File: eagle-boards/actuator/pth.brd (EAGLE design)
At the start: 59.4 x 53.3 mm, 9 parts, among them IC1 ULN2003AN, IC2 ULN2003AN

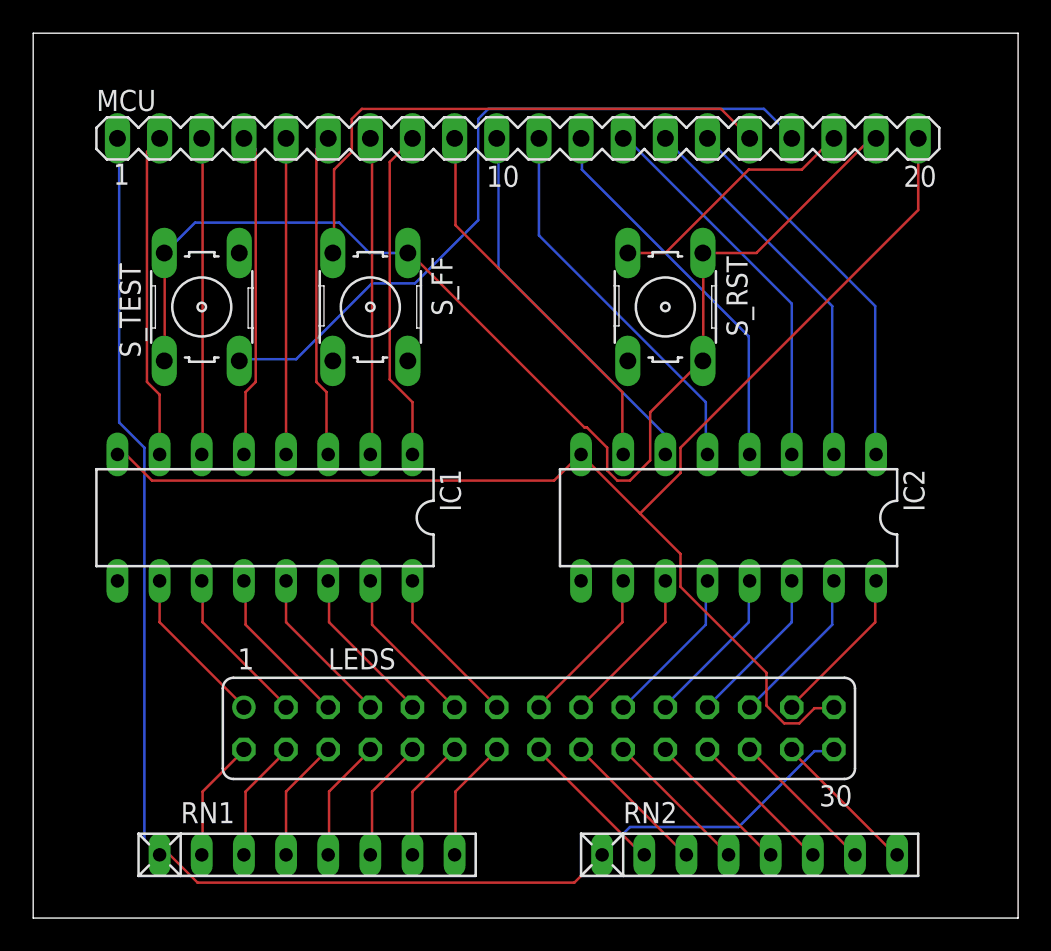
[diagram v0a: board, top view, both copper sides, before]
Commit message: New revision for the actuator board.
Fix orientation of buttons to be the same between all three, and include pull-down resistors if the input lines are not pulled down.
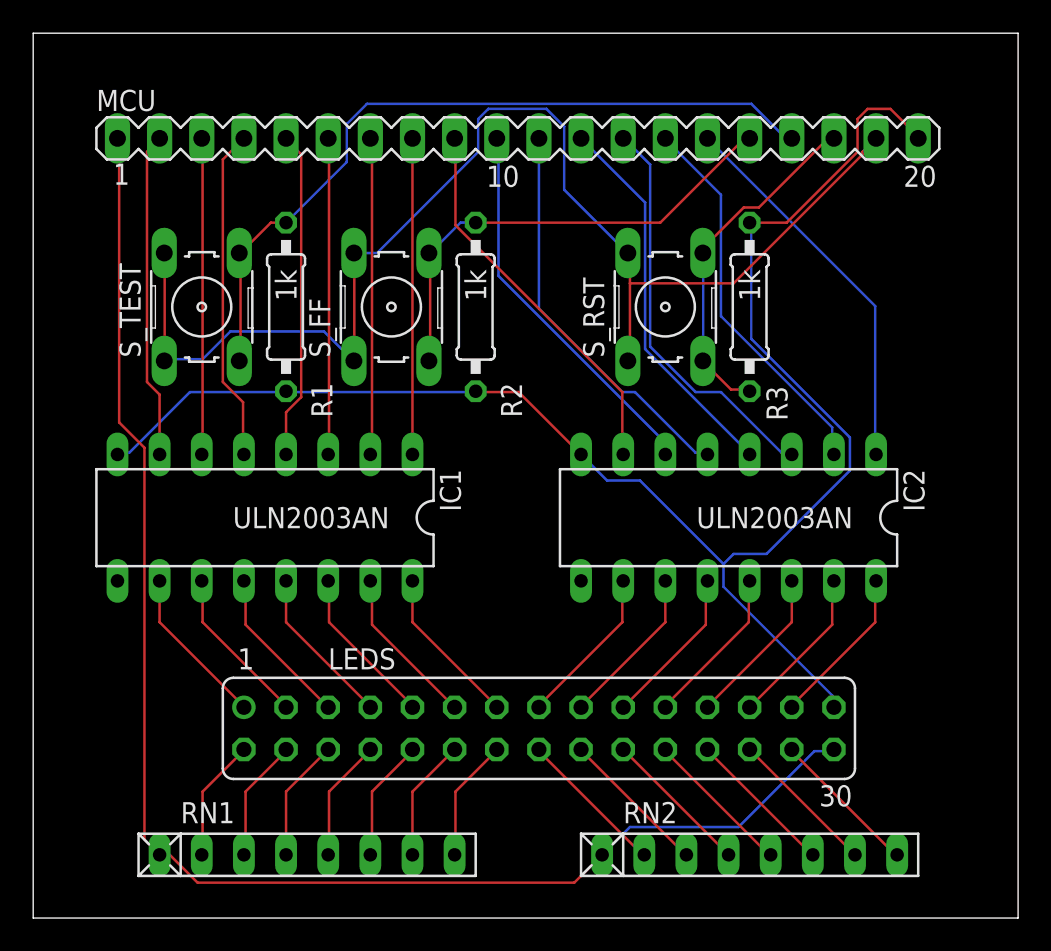
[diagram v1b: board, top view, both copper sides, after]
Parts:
- added R1, R2, R3: 1k, rcl:0207/10
- moved S_FF 1.27 mm to (21.6, 36.8), turned to 90 degrees
- turned S_RST to 90 degrees
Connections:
- net GND: now also R1.2, R2.2, R3.2
- net N$17: now also R3.1, S_RST.4
- net N$18: now also R1.1, S_TEST.4
- net N$19: now also R2.1, S_FF.4
- net N$2: now also S_FF.2
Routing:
- net GND: track 83.4 -> 96.3 mm
- net N$2: track 71.5 -> 78.3 mm
- net N$17: track 15.3 -> 21.1 mm
- net N$19: track 33.6 -> 28.8 mm
- net N$18: track 44.0 -> 45.8 mm
- net N$1: track 20.2 -> 19.1 mm
- net N$13: track 23.5 -> 24.5 mm
- net N$11: track 23.3 -> 24.1 mm
- net N$6: track 19.1 -> 19.8 mm
- net N$7: track 19.7 -> 19.1 mm
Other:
- board text added: "Birch Books Smart Home - Actuator Board (PTH) rev.2"
- board text added: "Copyright © 2020 D. E. Pettenò - flameeyes.com/p/birch-books Licensed under MIT License"
- board text removed: "Birch Books Smart Home Actuator Board (PTH) rev.1"
